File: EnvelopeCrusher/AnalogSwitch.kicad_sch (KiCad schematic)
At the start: 8 parts

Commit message: updated
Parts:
- gave numbers to parts that had none: 1
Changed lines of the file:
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@@
   (symbol (lib_id "4xxx:4066") (at 207.01 58.42 180) (unit 1)
     (in_bom yes) (on_board yes) (fields_autoplaced)
-    (property "Reference" "U?" (id 0) (at 207.01 50.8 0))
+    (property "Reference" "U5" (id 0) (at 207.01 50.8 0))
     (property "Value" "4066" (id 1) (at 207.01 53.34 0))
     (property "Footprint" "" (id 2) (at 207.01 58.42 0)
@@
   (symbol (lib_id "4xxx:4066") (at 207.01 119.38 180) (unit 3)
     (in_bom yes) (on_board yes) (fields_autoplaced)
-    (property "Reference" "U?" (id 0) (at 207.01 111.76 0))
+    (property "Reference" "U5" (id 0) (at 207.01 111.76 0))
     (property "Value" "4066" (id 1) (at 207.01 114.3 0))
     (property "Footprint" "" (id 2) (at 207.01 119.38 0)
@@
   (symbol (lib_id "4xxx:4066") (at 207.01 149.86 180) (unit 4)
     (in_bom yes) (on_board yes) (fields_autoplaced)
-    (property "Reference" "U?" (id 0) (at 207.01 142.24 0))
+    (property "Reference" "U5" (id 0) (at 207.01 142.24 0))
     (property "Value" "4066" (id 1) (at 207.01 144.78 0))
     (property "Footprint" "" (id 2) (at 207.01 149.86 0)
@@
   (symbol (lib_id "4xxx:4066") (at 189.23 214.63 90) (unit 5)
     (in_bom yes) (on_board yes) (fields_autoplaced)
-    (property "Reference" "U?" (id 0) (at 189.23 204.47 90))
+    (property "Reference" "U5" (id 0) (at 189.23 204.47 90))
     (property "Value" "4066" (id 1) (at 189.23 207.01 90))
     (property "Footprint" "" (id 2) (at 189.23 214.63 0)
@@
   (symbol (lib_id "4xxx:4066") (at 207.01 88.9 180) (unit 2)
     (in_bom yes) (on_board yes) (fields_autoplaced)
-    (property "Reference" "U?" (id 0) (at 207.01 81.28 0))
+    (property "Reference" "U5" (id 0) (at 207.01 81.28 0))
     (property "Value" "4066" (id 1) (at 207.01 83.82 0))
     (property "Footprint" "" (id 2) (at 207.01 88.9 0)

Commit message: Completed Schematic
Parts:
- C41, C43: renamed from C?; value ~ -> 1uF
- gave numbers to parts that had none: 1
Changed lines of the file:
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@@
   (symbol (lib_id "power:+5V") (at 157.48 208.9079 0) (unit 1)
     (in_bom yes) (on_board yes) (fields_autoplaced)
-    (property "Reference" "#PWR?" (id 0) (at 157.48 212.7179 0)
+    (property "Reference" "#PWR061" (id 0) (at 157.48 212.7179 0)
       (effects (font (size 1.27 1.27)) hide)
     )
@@
   (symbol (lib_id "Device:C") (at 144.78 224.79 180) (unit 1)
     (in_bom yes) (on_board yes)
-    (property "Reference" "C?" (id 0) (at 146.05 222.25 0)
+    (property "Reference" "C41" (id 0) (at 146.05 222.25 0)
       (effects (font (size 1.27 1.27)) (justify right))
     )
-    (property "Value" "~" (id 1) (at 146.05 228.6 0)
+    (property "Value" "1uF" (id 1) (at 146.05 228.6 0)
       (effects (font (size 1.27 1.27)) (justify right))
     )
@@
   (symbol (lib_id "power:-5V") (at 220.98 208.9079 0) (unit 1)
     (in_bom yes) (on_board yes) (fields_autoplaced)
-    (property "Reference" "#PWR?" (id 0) (at 220.98 206.3679 0)
+    (property "Reference" "#PWR062" (id 0) (at 220.98 206.3679 0)
       (effects (font (size 1.27 1.27)) hide)
     )
@@
   (symbol (lib_id "power:GND") (at 233.68 234.95 0) (unit 1)
     (in_bom yes) (on_board yes) (fields_autoplaced)
-    (property "Reference" "#PWR?" (id 0) (at 233.68 241.3 0)
+    (property "Reference" "#PWR063" (id 0) (at 233.68 241.3 0)
       (effects (font (size 1.27 1.27)) hide)
     )
@@
   (symbol (lib_id "power:GND") (at 144.78 234.95 0) (unit 1)
     (in_bom yes) (on_board yes) (fields_autoplaced)
-    (property "Reference" "#PWR?" (id 0) (at 144.78 241.3 0)
+    (property "Reference" "#PWR060" (id 0) (at 144.78 241.3 0)
       (effects (font (size 1.27 1.27)) hide)
     )
@@
   (symbol (lib_id "Device:C") (at 233.68 224.79 180) (unit 1)
     (in_bom yes) (on_board yes)
-    (property "Reference" "C?" (id 0) (at 234.95 222.25 0)
+    (property "Reference" "C43" (id 0) (at 234.95 222.25 0)
       (effects (font (size 1.27 1.27)) (justify right))
     )
-    (property "Value" "~" (id 1) (at 234.95 228.6 0)
+    (property "Value" "1uF" (id 1) (at 234.95 228.6 0)
       (effects (font (size 1.27 1.27)) (justify right))
     )
@@
   (symbol (lib_id "Device:C") (at 189.23 232.41 90) (unit 1)
     (in_bom yes) (on_board yes)
-    (property "Reference" "C?" (id 0) (at 189.23 228.6 90))
+    (property "Reference" "C42" (id 0) (at 189.23 228.6 90))
     (property "Value" "~" (id 1) (at 189.23 236.22 90))
     (property "Footprint" "" (id 2) (at 193.04 231.4448 0)

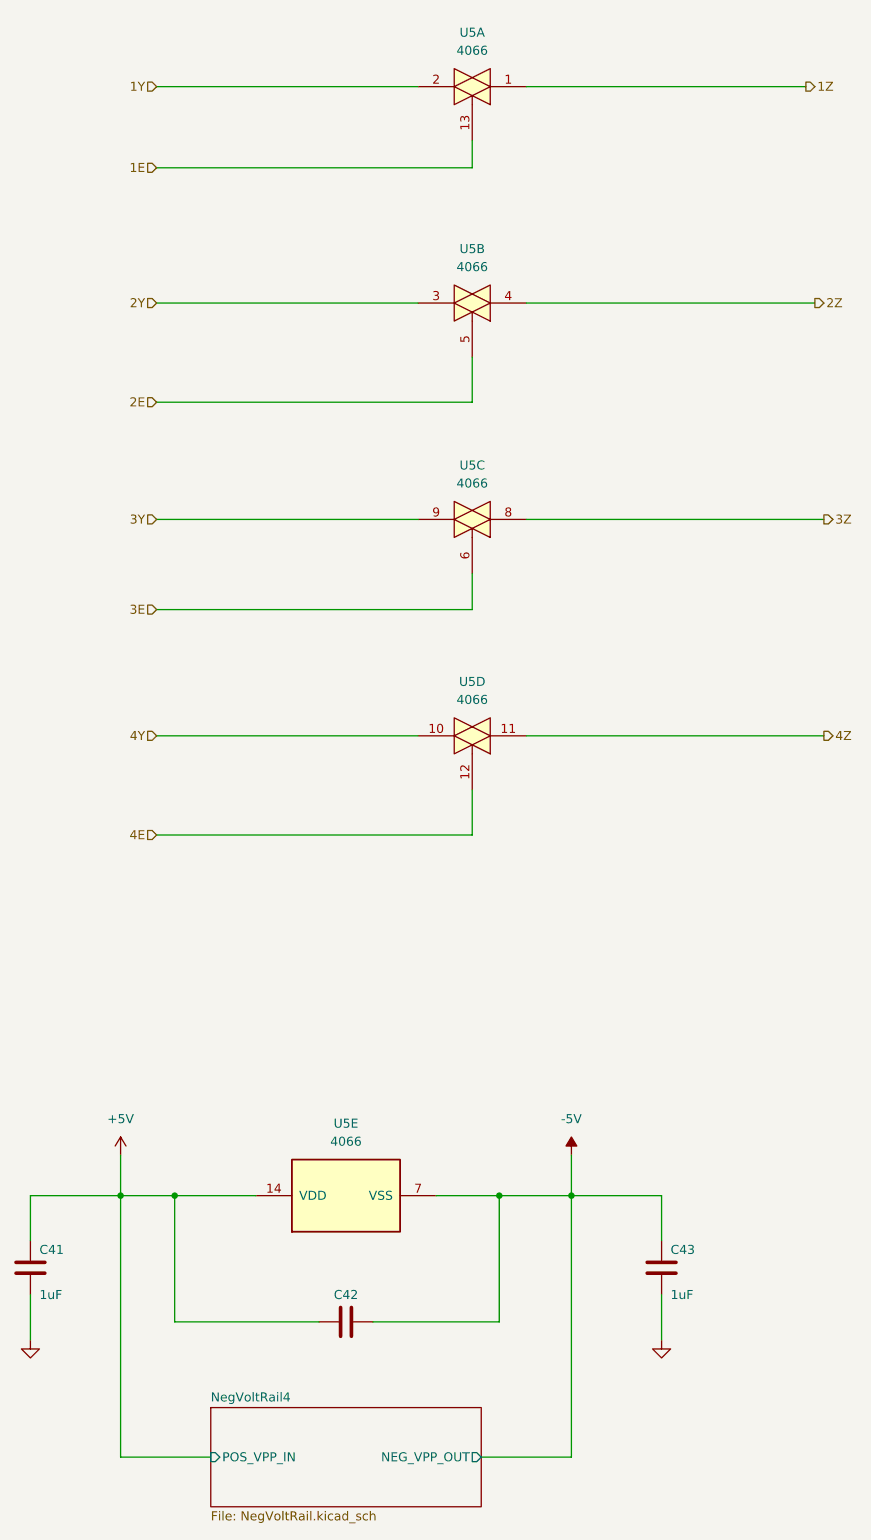
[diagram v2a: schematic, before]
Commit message: Updated schematic
- Replaced CD4066 (SOIC14) with DG611 (QFN16)
- Replaced CLK/ENV mixer jumpers with 4xSPST DIPSW
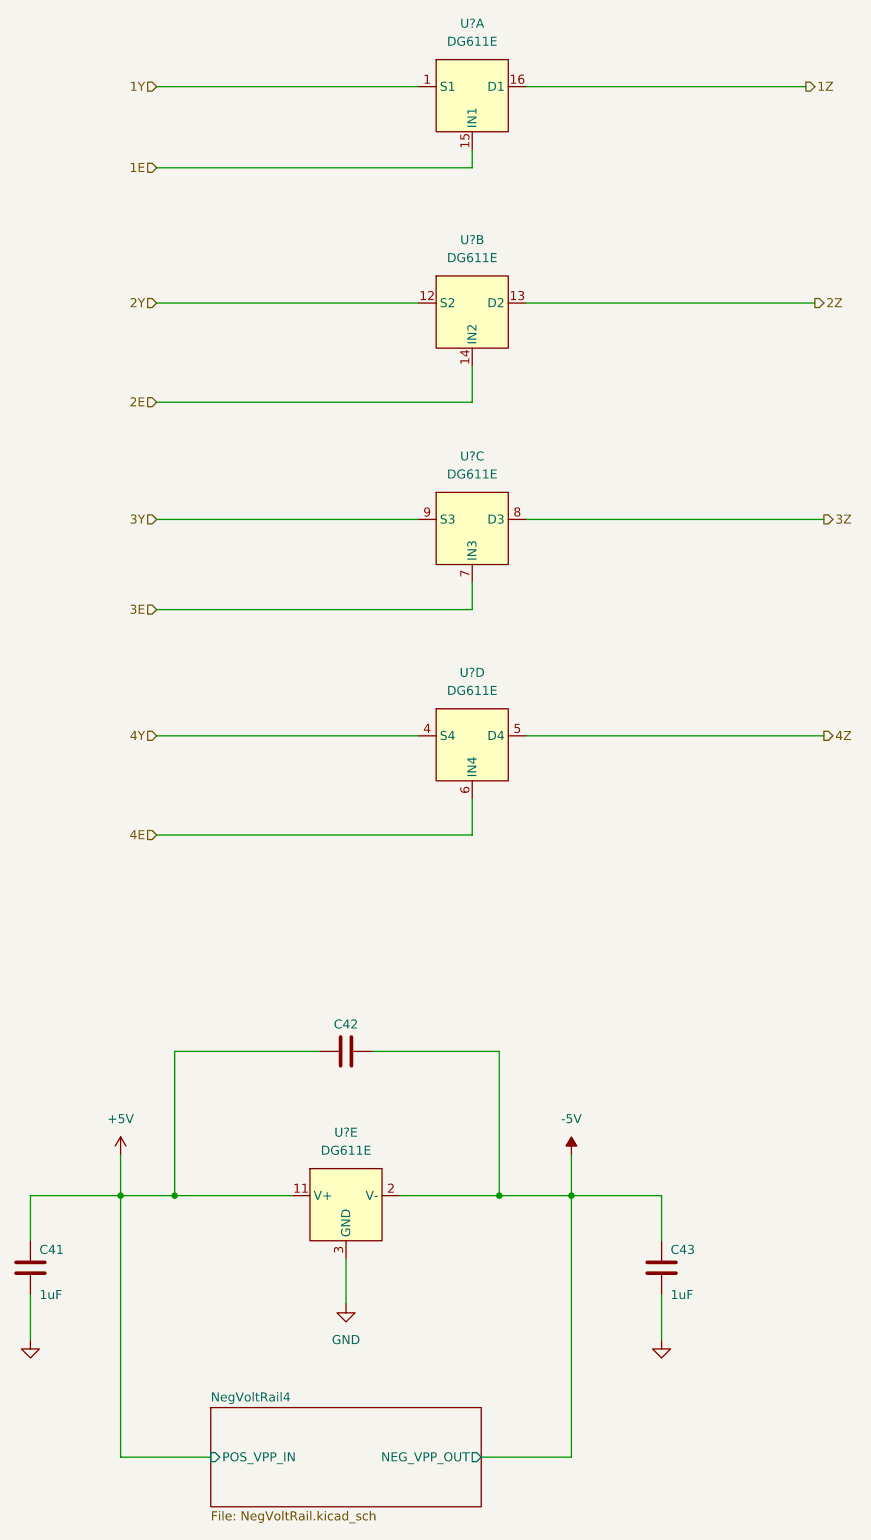
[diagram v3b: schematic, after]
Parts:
- removed U5: 4066, symbol 4xxx:4066
- added U?: DG611E, ThinMiniQFN:ThinMiniQFN-16_2.6mm_1.8mm, symbol DG61x:DG611E
- added U? (x4): DG611E, symbol DG61x:DG611E
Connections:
- net +5V: now also U?.11 (V+)
- net -5V: now also U?.2 (V-)
- net 1E: now also U?.15 (IN1)
- net 1Y: now also U?.1 (S1)
- net 1Z: now also U?.16 (D1)
- net 2E: now also U?.14 (IN2)
- net 2Y: now also U?.12 (S2)
- net 2Z: now also U?.13 (D2)
- net 3E: now also U?.7 (IN3)
- net 3Y: now also U?.9 (S3)
- net 3Z: now also U?.8 (D3)
- net 4E: now also U?.6 (IN4)
- net 4Y: now also U?.4 (S4)
- net 4Z: now also U?.5 (D4)
- net GND: now also U?.3 (GND)
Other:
- moved on the sheet: C42

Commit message: updated schematic
- Added values and comments to state-variable filter block
- Updated footprints
- Changed Dual Op Amp: TL072 to AM358
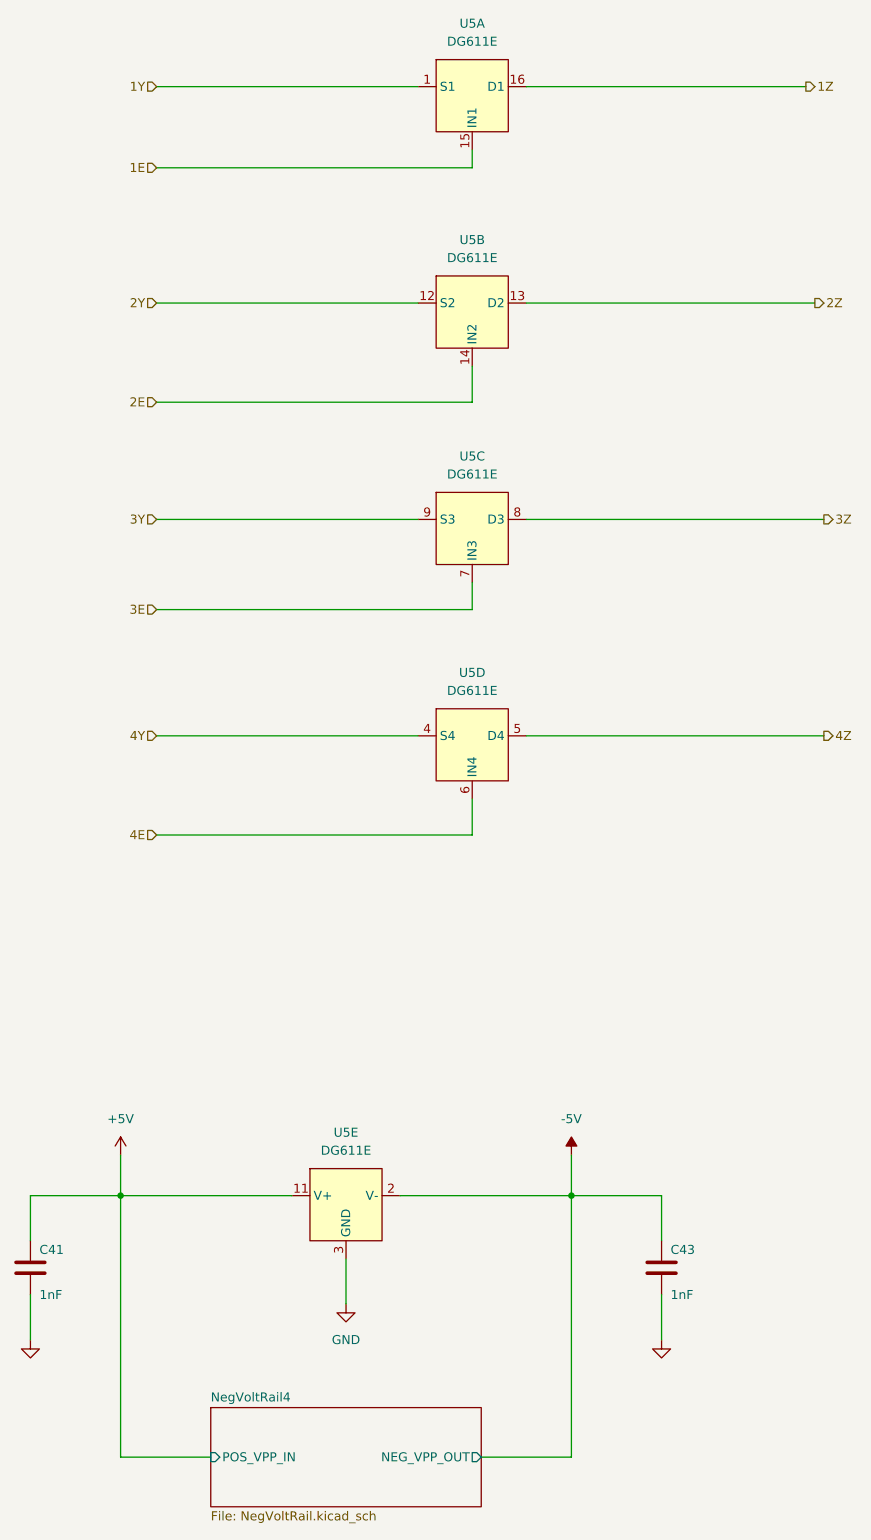
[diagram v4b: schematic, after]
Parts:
- removed C42: ~, symbol Device:C
- C41, C43: value 1uF -> 1nF; footprint (none) -> Capacitor_SMD:C_0805_2012Metric_Pad1.18x1.45mm_HandSolder
- U5: renamed from U?; footprint (none) -> ThinMiniQFN:ThinMiniQFN-16_2.6mm_1.8mm
- gave numbers to parts that had none: 1
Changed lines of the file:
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@@
 (kicad_sch (version 20211123) (generator eeschema)
   (paper "A3")
-  (junction (at 165.1 214.63) (diameter 0) (color 0 0 0 0)
-  )
   (junction (at 157.48 214.63) (diameter 0) (color 0 0 0 0)
   )
-  (junction (at 210.82 214.63) (diameter 0) (color 0 0 0 0)
-  )
   (junction (at 220.98 214.63) (diameter 0) (color 0 0 0 0)
   )
-  (wire (pts (xy 210.82 194.31) (xy 210.82 214.63))
-    (stroke (width 0) (type default) (color 0 0 0 0))
-  )
-  (wire (pts (xy 165.1 214.63) (xy 181.61 214.63))
+  (wire (pts (xy 157.48 214.63) (xy 181.61 214.63))
     (stroke (width 0) (type default) (color 0 0 0 0))
   )
@@
     (stroke (width 0) (type default) (color 0 0 0 0))
   )
-  (wire (pts (xy 196.85 214.63) (xy 210.82 214.63))
+  (wire (pts (xy 196.85 214.63) (xy 220.98 214.63))
     (stroke (width 0) (type default) (color 0 0 0 0))
   )
@@
     (stroke (width 0) (type default) (color 0 0 0 0))
   )
-  (wire (pts (xy 165.1 194.31) (xy 165.1 214.63))
-    (stroke (width 0) (type default) (color 0 0 0 0))
-  )
   (wire (pts (xy 162.56 88.9) (xy 199.39 88.9))
     (stroke (width 0) (type default) (color 0 0 0 0))
@@
     (stroke (width 0) (type default) (color 0 0 0 0))
   )
-  (wire (pts (xy 193.04 194.31) (xy 210.82 194.31))
-    (stroke (width 0) (type default) (color 0 0 0 0))
-  )
   (wire (pts (xy 162.56 102.87) (xy 207.01 102.87))
     (stroke (width 0) (type default) (color 0 0 0 0))
@@
     (stroke (width 0) (type default) (color 0 0 0 0))
   )
-  (wire (pts (xy 185.42 194.31) (xy 165.1 194.31))
-    (stroke (width 0) (type default) (color 0 0 0 0))
-  )
-  (wire (pts (xy 210.82 214.63) (xy 220.98 214.63))
-    (stroke (width 0) (type default) (color 0 0 0 0))
-  )
   (wire (pts (xy 220.98 251.46) (xy 208.28 251.46))
     (stroke (width 0) (type default) (color 0 0 0 0))
@@
   )
   (wire (pts (xy 144.78 228.6) (xy 144.78 234.95))
-    (stroke (width 0) (type default) (color 0 0 0 0))
-  )
-  (wire (pts (xy 157.48 214.63) (xy 165.1 214.63))
     (stroke (width 0) (type default) (color 0 0 0 0))
   )
@@
   (symbol (lib_name "DG611E_1") (lib_id "DG61x:DG611E") (at 189.23 214.63 0) (unit 5)
     (in_bom yes) (on_board yes) (fields_autoplaced)
-    (property "Reference" "U?" (id 0) (at 189.23 205.74 0))
+    (property "Reference" "U5" (id 0) (at 189.23 205.74 0))
     (property "Value" "DG611E" (id 1) (at 189.23 208.28 0))
     (property "Footprint" "ThinMiniQFN:ThinMiniQFN-16_2.6mm_1.8mm" (id 2) (at 189.23 214.63 0)
@@
   (symbol (lib_id "DG61x:DG611E") (at 207.01 88.9 0) (unit 2)
     (in_bom yes) (on_board yes) (fields_autoplaced)
-    (property "Reference" "U?" (id 0) (at 207.01 80.01 0))
+    (property "Reference" "U5" (id 0) (at 207.01 80.01 0))
     (property "Value" "DG611E" (id 1) (at 207.01 82.55 0))
-    (property "Footprint" "" (id 2) (at 207.01 88.9 0)
-      (effects (font (size 1.27 1.27)) hide)
-    )
-    (property "Datasheet" "" (id 3) (at 207.01 88.9 0)
+    (property "Footprint" "ThinMiniQFN:ThinMiniQFN-16_2.6mm_1.8mm" (id 2) (at 207.01 88.9 0)
+      (effects (font (size 1.27 1.27)) hide)
+    )
+    (property "Datasheet" "https://www.vishay.com/docs/78910/dg611e.pdf" (id 3) (at 207.01 88.9 0)
       (effects (font (size 1.27 1.27)) hide)
     )
@@
   (symbol (lib_id "DG61x:DG611E") (at 207.01 119.38 0) (unit 3)
     (in_bom yes) (on_board yes) (fields_autoplaced)
-    (property "Reference" "U?" (id 0) (at 207.01 110.49 0))
+    (property "Reference" "U5" (id 0) (at 207.01 110.49 0))
     (property "Value" "DG611E" (id 1) (at 207.01 113.03 0))
-    (property "Footprint" "" (id 2) (at 207.01 119.38 0)
-      (effects (font (size 1.27 1.27)) hide)
-    )
-    (property "Datasheet" "" (id 3) (at 207.01 119.38 0)
+    (property "Footprint" "ThinMiniQFN:ThinMiniQFN-16_2.6mm_1.8mm" (id 2) (at 207.01 119.38 0)
+      (effects (font (size 1.27 1.27)) hide)
+    )
+    (property "Datasheet" "https://www.vishay.com/docs/78910/dg611e.pdf" (id 3) (at 207.01 119.38 0)
       (effects (font (size 1.27 1.27)) hide)
     )
@@
       (effects (font (size 1.27 1.27)) (justify right))
     )
-    (property "Value" "1uF" (id 1) (at 146.05 228.6 0)
+    (property "Value" "1nF" (id 1) (at 146.05 228.6 0)
       (effects (font (size 1.27 1.27)) (justify right))
     )
-    (property "Footprint" "" (id 2) (at 143.8148 220.98 0)
+    (property "Footprint" "Capacitor_SMD:C_0805_2012Metric_Pad1.18x1.45mm_HandSolder" (id 2) (at 143.8148 220.98 0)
       (effects (font (size 1.27 1.27)) hide)
     )
@@
   (symbol (lib_id "DG61x:DG611E") (at 207.01 149.86 0) (unit 4)
     (in_bom yes) (on_board yes) (fields_autoplaced)
-    (property "Reference" "U?" (id 0) (at 207.01 140.97 0))
+    (property "Reference" "U5" (id 0) (at 207.01 140.97 0))
     (property "Value" "DG611E" (id 1) (at 207.01 143.51 0))
-    (property "Footprint" "" (id 2) (at 207.01 149.86 0)
-      (effects (font (size 1.27 1.27)) hide)
-    )
-    (property "Datasheet" "" (id 3) (at 207.01 149.86 0)
+    (property "Footprint" "ThinMiniQFN:ThinMiniQFN-16_2.6mm_1.8mm" (id 2) (at 207.01 149.86 0)
+      (effects (font (size 1.27 1.27)) hide)
+    )
+    (property "Datasheet" "https://www.vishay.com/docs/78910/dg611e.pdf" (id 3) (at 207.01 149.86 0)
       (effects (font (size 1.27 1.27)) hide)
     )
@@
   (symbol (lib_id "DG61x:DG611E") (at 207.01 58.42 0) (unit 1)
     (in_bom yes) (on_board yes) (fields_autoplaced)
-    (property "Reference" "U?" (id 0) (at 207.01 49.53 0))
+    (property "Reference" "U5" (id 0) (at 207.01 49.53 0))
     (property "Value" "DG611E" (id 1) (at 207.01 52.07 0))
-    (property "Footprint" "" (id 2) (at 207.01 58.42 0)
-      (effects (font (size 1.27 1.27)) hide)
-    )
-    (property "Datasheet" "" (id 3) (at 207.01 58.42 0)
+    (property "Footprint" "ThinMiniQFN:ThinMiniQFN-16_2.6mm_1.8mm" (id 2) (at 207.01 58.42 0)
+      (effects (font (size 1.27 1.27)) hide)
+    )
+    (property "Datasheet" "https://www.vishay.com/docs/78910/dg611e.pdf" (id 3) (at 207.01 58.42 0)
       (effects (font (size 1.27 1.27)) hide)
     )
@@
   (symbol (lib_id "power:GND") (at 189.23 229.87 0) (unit 1)
     (in_bom yes) (on_board yes) (fields_autoplaced)
-    (property "Reference" "#PWR?" (id 0) (at 189.23 236.22 0)
+    (property "Reference" "#PWR0100" (id 0) (at 189.23 236.22 0)
       (effects (font (size 1.27 1.27)) hide)
     )
@@
       (effects (font (size 1.27 1.27)) (justify right))
     )
-    (property "Value" "1uF" (id 1) (at 234.95 228.6 0)
+    (property "Value" "1nF" (id 1) (at 234.95 228.6 0)
       (effects (font (size 1.27 1.27)) (justify right))
     )
-    (property "Footprint" "" (id 2) (at 232.7148 220.98 0)
+    (property "Footprint" "Capacitor_SMD:C_0805_2012Metric_Pad1.18x1.45mm_HandSolder" (id 2) (at 232.7148 220.98 0)
       (effects (font (size 1.27 1.27)) hide)
     )
@@
       (effects (font (size 1.27 1.27)) hide)
     )
-    (pin "1")
-    (pin "2")
-  )
-  (symbol (lib_id "Device:C") (at 189.23 194.31 90) (unit 1)
-    (in_bom yes) (on_board yes)
-    (property "Reference" "C42" (id 0) (at 189.23 190.5 90))
-    (property "Value" "~" (id 1) (at 189.23 198.12 90))
-    (property "Footprint" "" (id 2) (at 193.04 193.3448 0)
-      (effects (font (size 1.27 1.27)) hide)
-    )
-    (property "Datasheet" "~" (id 3) (at 189.23 194.31 0)
-      (effects (font (size 1.27 1.27)) hide)
-    )
